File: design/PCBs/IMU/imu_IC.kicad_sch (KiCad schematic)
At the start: 9 parts, among them J1 Conn_01x04, J2 Conn_01x04, U1 ISM330DHCX

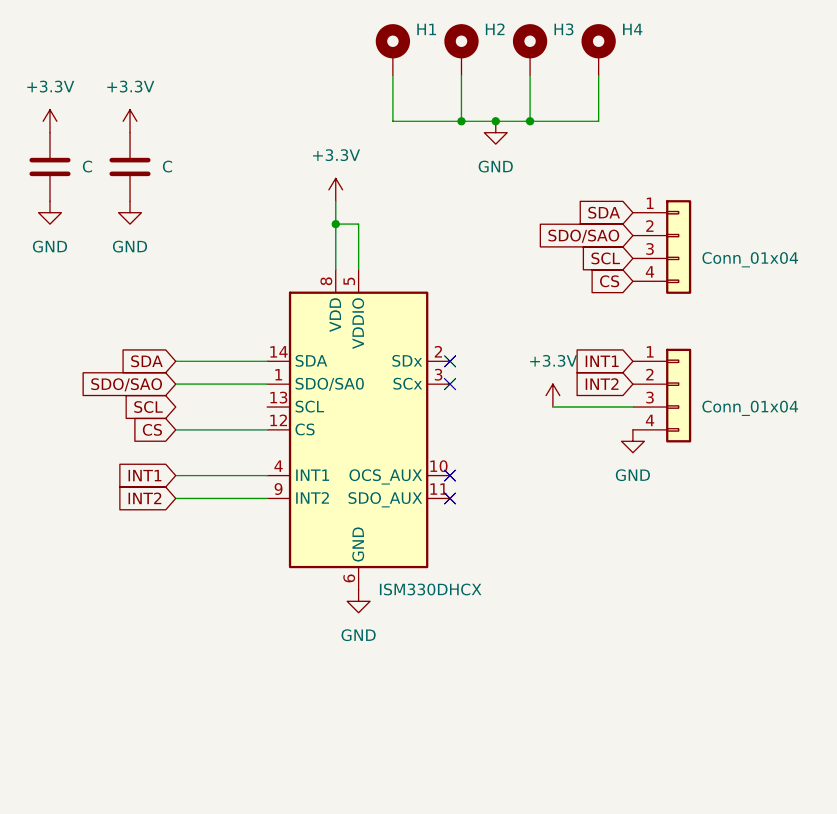
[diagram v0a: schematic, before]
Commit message: Added micro-servo headers Added header for FFC cable IMU PCB
We need to set IMU PCB input to correspond to
the one we have made here.
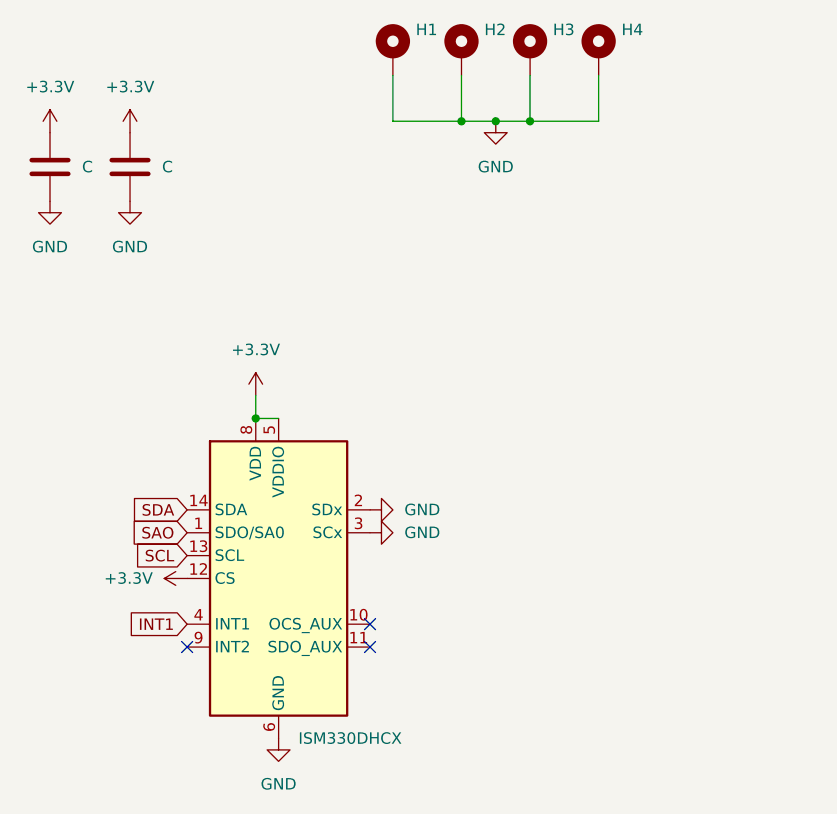
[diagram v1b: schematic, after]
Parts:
- removed J1, J2: Conn_01x04, Connector:FanPinHeader_1x04_P2.54mm_Vertical, symbol Connector_Generic:Conn_01x04
- removed U1: ISM330DHCX, Package_LGA:LGA-14_3x2.5mm_P0.5mm_LayoutBorder3x4y, symbol Sensor_Motion:ISM330DHCX
- added U2: ISM330DHCX, Package_LGA:LGA-14_3x2.5mm_P0.5mm_LayoutBorder3x4y, symbol Sensor_Motion:ISM330DHCX
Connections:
- net +3.3V: now also U2.12 (CS), U2.5 (VDDIO), U2.8 (VDD)
- net GND: now also U2.2 (SDx), U2.3 (SCx), U2.6 (GND), U2.7 (GND)
- net INT1: now also U2.4 (INT1)
- net SCL: now also U2.13 (SCL)
- net SDA: now also U2.14 (SDA)
- new net SAO: U2.1 (SDO/SA0)
- no-connect marks 4 -> 3
